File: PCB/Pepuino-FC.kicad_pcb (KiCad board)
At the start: 2 copper layers, 46.1 x 70 mm, 101 parts, among them CN1 XT30UPB-M, M1 Motor_Servo, M2 Motor_Servo, M3 Motor_Servo, M4 Motor_Servo, M5 Motor_Servo, M6 Motor_Servo, Q1 IRLML6402TRPBF-JSM, Q2 IRLML6402TRPBF-JSM, SW1 TS-1088-AR02016, SW2 TS-1088-AR02016, U1 STM32F722RETx, U2 BQ25883RGER, U3 BMP580, U4 ICM-45686, U6 LMR51430, U7 RA-02, X1 Q13FC1350000400, X2 X322525MOB4SI

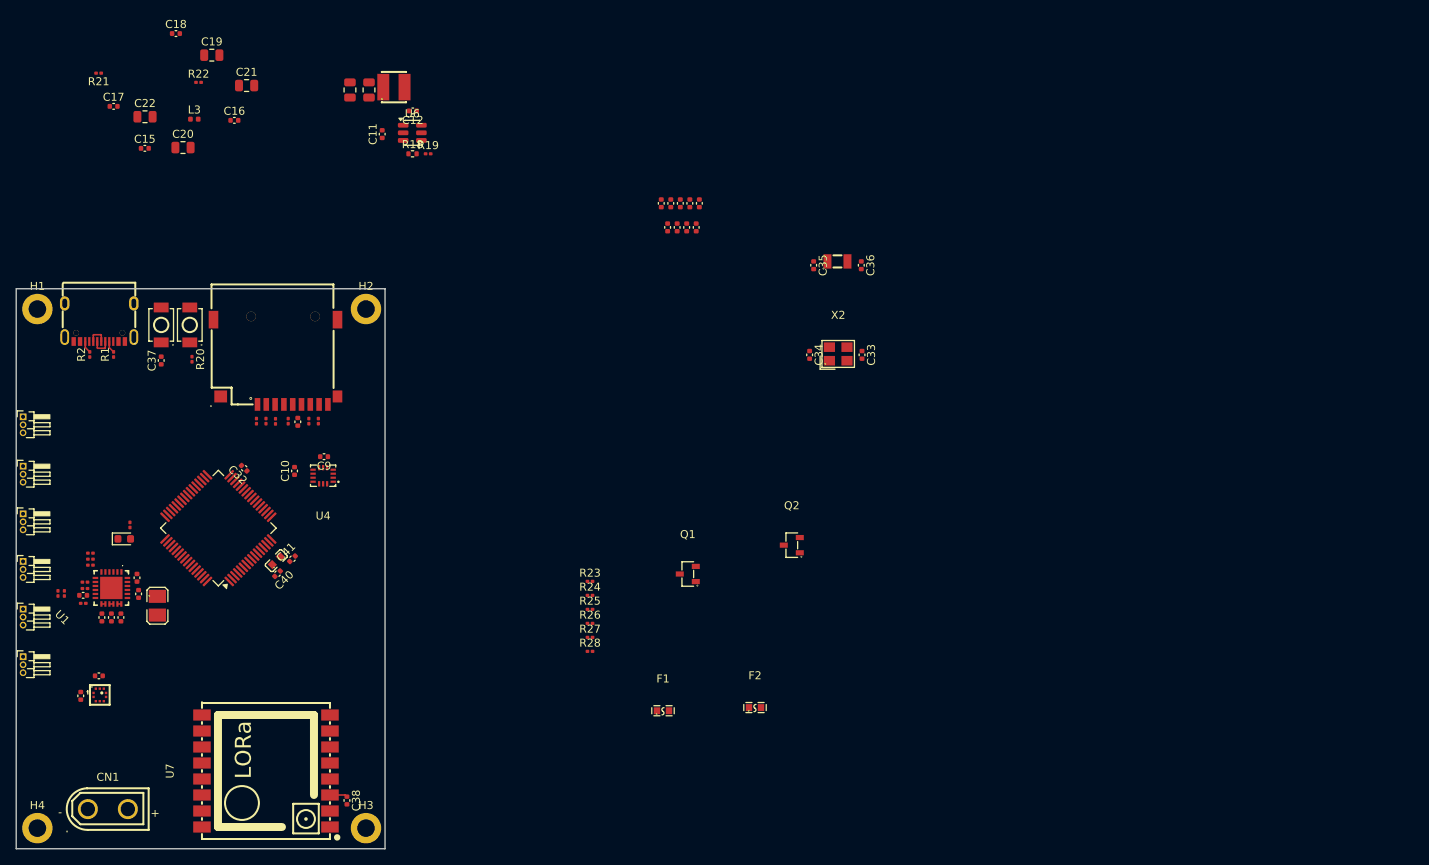
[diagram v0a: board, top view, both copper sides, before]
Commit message: update schematic
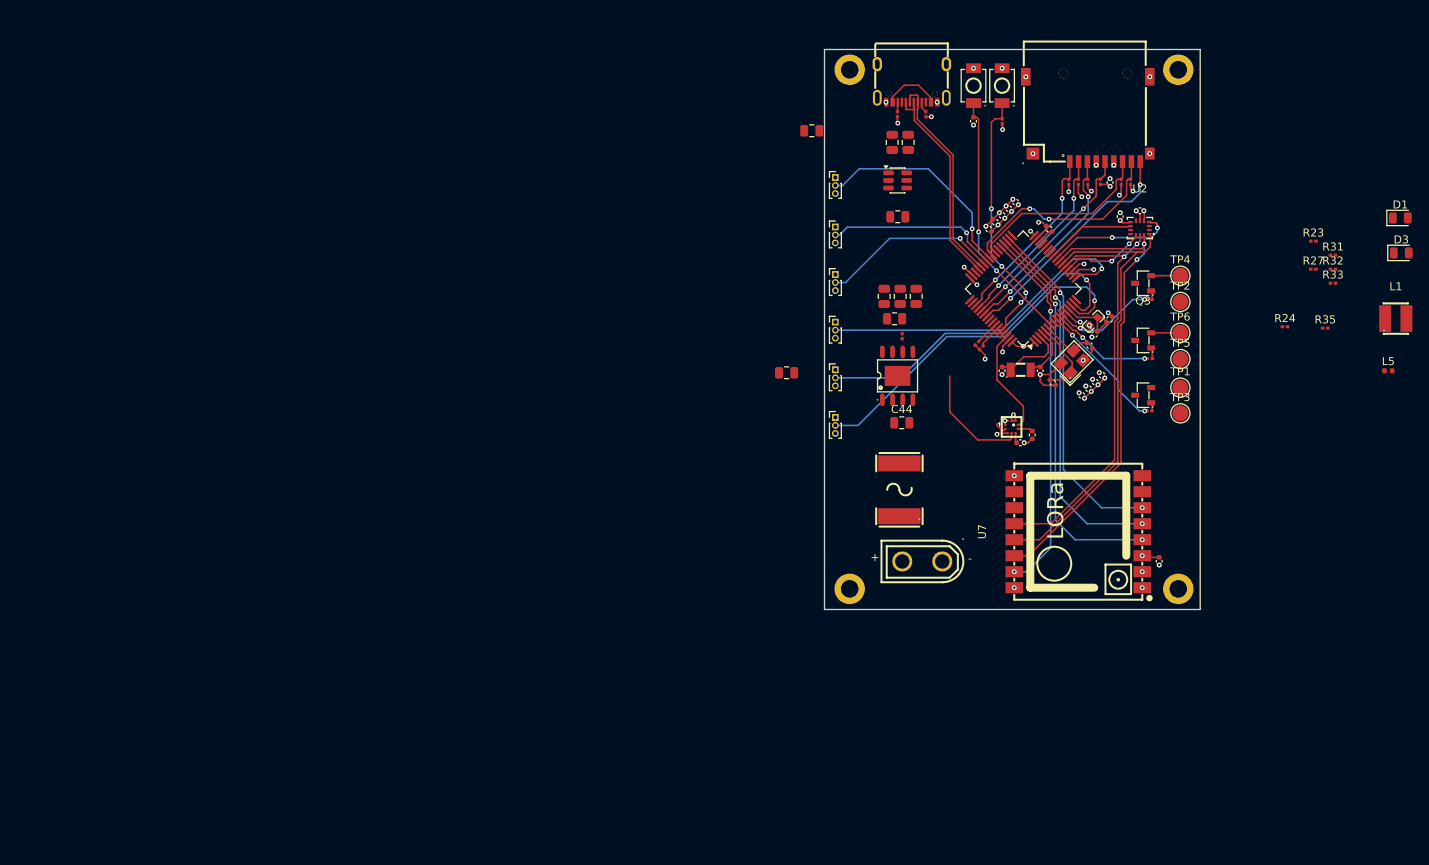
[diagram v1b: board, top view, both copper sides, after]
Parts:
- removed C1: 1nF, Capacitor_SMD:C_0402_1005Metric
- removed C11: 2.2uF, Capacitor_SMD:C_0402_1005Metric
- removed C12, C18: 0.1uF, Capacitor_SMD:C_0402_1005Metric
- removed C13, C14, C20, C21, C22: 22uF, Capacitor_SMD:C_0805_2012Metric
- removed C15, C16, C17: 10nF, Capacitor_SMD:C_0402_1005Metric
- removed C19: 10uF, Capacitor_SMD:C_0805_2012Metric
- removed C2, C4, C6: 10uF, Capacitor_SMD:C_0402_1005Metric
- removed C3: 44uF, Capacitor_SMD:C_0402_1005Metric
- removed C5: 47nF, Capacitor_SMD:C_0402_1005Metric
- removed F1, F2: 0438005.WRGT, easyEDA:F0603
- removed L2: YHNR3015-5R6M, easyEDA:IND-SMD_L3.0-W3.0
- removed L3: 1uH, Inductor_SMD:L_0402_1005Metric
- removed R10, R21, R22, R3, R4, R5, R6, R7: 10K, Resistor_SMD:R_0201_0603Metric
- removed R11: 383, Resistor_SMD:R_0201_0603Metric
- removed R18: 100K, Resistor_SMD:R_0402_1005Metric
- removed R19: 22.1K, Resistor_SMD:R_0201_0603Metric
- removed R8: 5.23K, Resistor_SMD:R_0201_0603Metric
- removed R9: 30.1K, Resistor_SMD:R_0201_0603Metric
- added C44: 10uF, Capacitor_SMD:C_0805_2012Metric, F.Cu at (140.2, 98.8)
- added C45: 0.1uF, Capacitor_SMD:C_0805_2012Metric, F.Cu at (125.8, 92.5)
- added C46: 2.7nF, Capacitor_SMD:C_0805_2012Metric, F.Cu at (139.3, 85.8)
- added C47: 22uF, Capacitor_SMD:C_0805_2012Metric, F.Cu at (138.0, 82.9)
- added C48: 22uF, Capacitor_SMD:C_0805_2012Metric, F.Cu at (140.0, 82.9)
- added C49: 22uF, Capacitor_SMD:C_0805_2012Metric, F.Cu at (142.0, 82.9)
- added C50: 22uF, Capacitor_SMD:C_0805_2012Metric, F.Cu at (139.7, 73.0)
- added C51: 0.1uF, Capacitor_SMD:C_0805_2012Metric, F.Cu at (128.9, 62.2)
- added C52: 22uF, Capacitor_SMD:C_0805_2012Metric, F.Cu at (139.0, 63.7)
- added C53: 22uF, Capacitor_SMD:C_0805_2012Metric, F.Cu at (141.0, 63.7)
- added D3: Green, LED_SMD:LED_0805_2012Metric, F.Cu at (202.6, 77.5)
- added L5: 3.6uH, Inductor_SMD:L_0402_1005Metric, F.Cu at (201.0, 92.2)
- added Q3: IRLML6402TRPBF-JSM, easyEDA:SOT-23-3_L2.9-W1.3-P1.90-LS2.4-BR, F.Cu at (170.4, 88.5)
- added R29: 4.7K, Resistor_SMD:R_0201_0603Metric, F.Cu at (149.6, 88.8)
- added R30: 4.7K, Resistor_SMD:R_0201_0603Metric, F.Cu at (150.1, 89.4)
- added R31: 22.1K, Resistor_SMD:R_0201_0603Metric, F.Cu at (194.1, 77.8)
- added R32: 100K, Resistor_SMD:R_0201_0603Metric, F.Cu at (194.1, 79.6)
- added R33: 220, Resistor_SMD:R_0201_0603Metric, F.Cu at (194.1, 81.3)
- added R34: 100, Resistor_SMD:R_0201_0603Metric, F.Cu at (171.2, 90.7)
- added R35: 56, Resistor_SMD:R_0201_0603Metric, F.Cu at (193.1, 86.9)
- added TP1: TestPoint, TestPoint:TestPoint_Pad_D2.0mm, F.Cu at (175.0, 94.4)
- added TP2: TestPoint, TestPoint:TestPoint_Pad_D2.0mm, F.Cu at (175.0, 83.6)
- added TP3: TestPoint, TestPoint:TestPoint_Pad_D2.0mm, F.Cu at (175.0, 97.6)
- added TP4: TestPoint, TestPoint:TestPoint_Pad_D2.0mm, F.Cu at (175.0, 80.4)
- added TP5: TestPoint, TestPoint:TestPoint_Pad_D2.0mm, F.Cu at (175.0, 90.8)
- added TP6: TestPoint, TestPoint:TestPoint_Pad_D2.0mm, F.Cu at (175.0, 87.5)
- added U9: BSMD2920-500-30V, easyEDA:F2920, F.Cu at (139.9, 107.1)
- D1: value LED -> Blue; footprint LED_SMD:LED_0603_1608Metric -> LED_SMD:LED_0805_2012Metric
- L1: value DFE252012F-1R0M=P2 -> YHNR3015-5R6M; footprint easyEDA:L2520 -> easyEDA:IND-SMD_L3.0-W3.0
- M1, M2, M3, M4, M5, M6: footprint Connector_PinHeader_1.00mm:PinHeader_1x03_P1.00mm_Horizontal -> Connector_PinHeader_1.00mm:PinHeader_1x03_P1.00mm_Vertical
- R23: value 10K -> 200K
- R24: value 1K -> 115K
- R27: value 10K -> 22.1K
- R28: value 1K -> 15.8K
- U2: value BQ25883RGER -> BMI270; footprint easyEDA:VFQFPN-24_L4.0-W4.0-P0.50-BL-EP2.8 -> easyEDA:LGA-14_L3.0-W2.5-P0.50-BR
- U4: value ICM-45686 -> LMR51430; footprint easyEDA:LGA-14_L3.0-W2.5-P0.50-TL -> Package_TO_SOT_SMD:SOT-23-6
- U6: value LMR51430 -> AP64500SP-13; footprint Package_TO_SOT_SMD:SOT-23-6 -> easyEDA:SO-8_L4.9-W3.9-P1.27-LS6.0-BL-EP
- moved D1 164.5 mm to (202.5, 73.2)
- moved L1 158.9 mm to (201.9, 85.7), turned to 0 degrees
- moved U2 136.2 mm to (170.0, 74.4), turned to 0 degrees
- moved C7 121.6 mm to (155.0, 101.2), turned to 180 degrees
- moved C8 120.5 mm to (156.5, 100.3), turned to 90 degrees
- moved U3 118.8 mm to (153.9, 99.3)
- moved C10 108.0 mm to (167.5, 73.0)
- moved C9 106.5 mm to (170.0, 72.2)
- moved C40 106.4 mm to (164.3, 87.7)
- moved C41 106.4 mm to (166.2, 85.8)
- moved L4 106.4 mm to (164.1, 86.1)
- moved CN1 106.4 mm to (142.8, 116.1), turned to 180 degrees
- moved Card1 106.0 mm to (163.4, 60.8)
- moved R1 105.9 mm to (143.2, 60.2)
- moved USB1 105.9 mm to (141.4, 56.3)
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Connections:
- C34 pad 1: Net-(C34-Pad1) -> /HSE_IN
- CN1 pad 1: PGND -> GND
- CN1 pad 2: BAT+ -> Net-(CN1-+)
- D1 pad 1: Net-(D1-K) -> GND
- L1 pad 1: Net-(C2-Pad1) -> Net-(U4-SW)
- L1 pad 2: /BTST -> +3V3
- M1 pad 1: +5V -> +5V_SERVO
- M2 pad 1: +5V -> +5V_SERVO
- M3 pad 1: +5V -> +5V_SERVO
- M4 pad 1: +5V -> +5V_SERVO
- M5 pad 1: +5V -> +5V_SERVO
- M6 pad 1: +5V -> +5V_SERVO
- Q1 pad 3: Net-(Q1-D) -> GND
- Q2 pad 3: Net-(Q2-D) -> GND
- R23 pad 1: BAT+ -> Net-(U6-RT/CLK)
- R23 pad 2: Net-(Q1-D) -> GND
- R24 pad 1: Net-(Q1-D) -> Net-(U6-FB)
- R24 pad 2: Net-(D3-A) -> +5V_SERVO
- R26 pad 1: /PYRO_2 -> /PYRO_3
- R27 pad 1: BAT+ -> GND
- R27 pad 2: Net-(Q2-D) -> Net-(U6-FB)
- R28 pad 1: Net-(Q2-D) -> Net-(U6-COMP)
- U1 pad 10: unconnected-(U1-PC2-Pad10) -> /PYRO_2
- U1 pad 11: unconnected-(U1-PC3-Pad11) -> /PYRO_1
- U1 pad 14: /SERVO1 -> /SERVO6
- U1 pad 15: /SERVO2 -> /SERVO5
- U1 pad 16: /SERVO3 -> unconnected-(U1-PA2-Pad16)
- U1 pad 26: /PYRO_1 -> unconnected-(U1-PB1-Pad26)
- U1 pad 27: /PYRO_2 -> unconnected-(U1-PB2-Pad27)
- U1 pad 41: /SERVO5 -> /SERVO1
- U1 pad 42: /SERVO6 -> /SERVO2
- U1 pad 43: unconnected-(U1-PA10-Pad43) -> /SERVO3
- U1 pad 44: /USD_DP -> /USD_DN
- U1 pad 45: /USD_DN -> /USD_DP
- U1 pad 5: GND -> /HSE_IN
- U1 pad 9: unconnected-(U1-PC1-Pad9) -> /PYRO_3
- U2 pad 1: unconnected-(U2-D--Pad1) -> /MISO
- U2 pad 11: VREGN -> unconnected-(U2-OSDO-Pad11)
- U2 pad 12: Net-(U2-BTST) -> /BMI_CS
- U2 pad 13: BAT+ -> /SCK
- U2 pad 14: BAT+ -> /MOSI
- U2 pad 2: Net-(D1-K) -> unconnected-(U2-ASDX-Pad2)
- U2 pad 3: /BQ_CE -> unconnected-(U2-ASCX-Pad3)
- U2 pad 4: /I2C_SDA -> /BMI_INT
- U2 pad 5: /I2C_SCL -> +3V3
- U2 pad 6: /BQ_INT -> GND
- U2 pad 7: Net-(U2-TS) -> GND
- U2 pad 8: Net-(U2-ILIM) -> +3V3
- U2 pad 9: /BQ_PG -> /BMI_INT2
- U4 pad 1: /MISO -> GND
- U4 pad 2: unconnected-(U4-RESV/AUX1_SDIO/AUX1_SDI/MAS_DA-Pad2) -> Net-(U4-SW)
- U4 pad 3: unconnected-(U4-RESV/AUX1_SCLK/MAS_CLK-Pad3) -> VBAT
- U4 pad 4: /ICM_INT -> Net-(U4-FB)
- U4 pad 5: +3V3 -> VBAT
- U4 pad 6: GND -> Net-(U4-CB)
- U6 pad 1: GND -> Net-(U6-BST)
- U6 pad 2: Net-(U6-SW) -> VBAT
- U6 pad 3: VSYS -> VBAT
- U6 pad 4: Net-(U6-FB) -> Net-(U6-RT/CLK)
- U6 pad 5: VSYS -> Net-(U6-FB)
- U6 pad 6: Net-(U6-CB) -> Net-(U6-COMP)
- X2 pad 1: GND -> /HSE_IN
- X2 pad 4: Net-(C34-Pad1) -> GND
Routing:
- net +3V3: track 2.21 -> 204.2 mm, vias 0 -> 27
- net /MOSI: track 0.00 -> 59.3 mm, vias 0 -> 2
- net /MISO: track 0.00 -> 58.0 mm
- net /SCK: track 0.00 -> 53.0 mm, vias 0 -> 2
- net /RF_RESET: track 0.00 -> 49.1 mm, vias 0 -> 2
- net +5V_SERVO: track 0.00 -> 48.0 mm
- net /RF_DIO0: track 0.00 -> 46.4 mm, vias 0 -> 2
- net /RF_CS: track 0.00 -> 45.9 mm, vias 0 -> 2
- net /SERVO6: track 0.00 -> 45.2 mm, vias 0 -> 1
- net /RF_DIO1: track 0.00 -> 43.5 mm, vias 0 -> 2
- net /SERVO5: track 0.00 -> 43.1 mm, vias 0 -> 1
- net /SERVO4: track 0.00 -> 41.3 mm, vias 0 -> 1
- net GND: track 0.00 -> 36.1 mm, vias 0 -> 40
- net /BOOT: track 0.00 -> 32.6 mm, vias 0 -> 4
- net /RESET: track 0.00 -> 32.0 mm, vias 0 -> 2
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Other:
- board size 46.1 x 70 mm -> 47 x 70 mm
- copper layers 2 -> 4

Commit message: add final schematic
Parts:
- moved L1 68.1 mm to (136.3, 67.6)
- moved D1 67.7 mm to (135.5, 83.0), turned to 90 degrees
- moved D3 66.9 mm to (137.2, 63.7), turned to 90 degrees
- moved R35 59.7 mm to (138.6, 62.7), turned to 90 degrees
- moved R33 57.2 mm to (136.9, 82.1), turned to 90 degrees
- moved L5 56.6 mm to (144.6, 87.9)
- moved R23 54.2 mm to (141.9, 97.5), turned to -90 degrees
- moved R32 50.2 mm to (145.2, 68.3), turned to 90 degrees
- moved R31 49.6 mm to (145.2, 69.7), turned to 90 degrees
- moved R27 49.2 mm to (143.4, 89.3), turned to -90 degrees
- moved R24 44.8 mm to (143.4, 90.7), turned to -90 degrees
- moved C51 12.9 mm to (141.1, 66.6), turned to 180 degrees
- moved C45 10.5 mm to (136.3, 93.1), turned to 90 degrees
- moved C7 4.44 mm to (151.5, 98.6)
- moved U3 4.44 mm to (150.4, 96.6)
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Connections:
- M1 pad 1: +5V_SERVO -> /SERVO1
- M1 pad 2: /SERVO1 -> +5V_SERVO
- M2 pad 1: +5V_SERVO -> /SERVO2
- M2 pad 2: /SERVO2 -> +5V_SERVO
- M3 pad 1: +5V_SERVO -> /SERVO3
- M3 pad 2: /SERVO3 -> +5V_SERVO
- M4 pad 1: +5V_SERVO -> /SERVO4
- M4 pad 2: /SERVO4 -> +5V_SERVO
- M5 pad 1: +5V_SERVO -> /SERVO5
- M5 pad 2: /SERVO5 -> +5V_SERVO
- M6 pad 1: +5V_SERVO -> /SERVO6
- M6 pad 2: /SERVO6 -> +5V_SERVO
- U1 pad 20: /ICM_CS -> /BMI_CS
- U1 pad 24: /ICM_INT -> /BMI_INT
- U1 pad 25: /ICM_INT2 -> /BMI_INT2
- U1 pad 57: /BQ_INT -> unconnected-(U1-PB5-Pad57)
- U1 pad 61: /BQ_CE -> unconnected-(U1-PB8-Pad61)
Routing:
- net +3V3: track 204.2 -> 0.00 mm, vias 27 -> 0
- net /MOSI: track 59.3 -> 0.00 mm, vias 2 -> 0
- net /MISO: track 58.0 -> 0.00 mm
- net /SCK: track 53.0 -> 0.00 mm, vias 2 -> 0
- net /RF_RESET: track 49.1 -> 0.00 mm, vias 2 -> 0
- net +5V_SERVO: track 48.0 -> 0.00 mm
- net /RF_DIO0: track 46.4 -> 0.00 mm, vias 2 -> 0
- net /RF_CS: track 45.9 -> 0.00 mm, vias 2 -> 0
- net /SERVO6: track 45.2 -> 0.00 mm, vias 1 -> 0
- net /RF_DIO1: track 43.5 -> 0.00 mm, vias 2 -> 0
- net /SERVO5: track 43.1 -> 0.00 mm, vias 1 -> 0
- net /SERVO4: track 41.3 -> 0.00 mm, vias 1 -> 0
- net GND: track 36.1 -> 0.00 mm, vias 40 -> 0
- net /BOOT: track 32.6 -> 0.00 mm, vias 4 -> 0
- net /RESET: track 32.0 -> 0.00 mm, vias 2 -> 0
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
